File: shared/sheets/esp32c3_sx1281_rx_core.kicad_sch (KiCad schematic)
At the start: 36 parts, among them U1 ESP32-C3FH4, U2 TLV75533PDQNR, U3 SX1281IMLTRT, X1 CJ17-400001010B20

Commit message: Switch passives to 0201 with correct LCSC basic parts
- 100nF: C14858 (0201 X5R 6.3V)
- 1uF: C77857 (0201 X5R 6.3V)
- 10pF: C14854 (0201 C0G 25V)
- 470nF: C304534 (0201 X5R 6.3V)
- 1nF: C80390 (0201 X7R 25V)
- 10k: C172043 (0201 1%)
- 10uF: C15525 (0603 X5R 10V, no 0201 available)
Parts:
- C1, C13, C14, C15, C17, C2, C3, C4, C5: footprint Capacitor_SMD:C_0402_1005Metric -> Capacitor_SMD:C_0201_0603Metric; LCSC C1525 -> C14858
- C10, C19, C8, C9: footprint Capacitor_SMD:C_0402_1005Metric -> Capacitor_SMD:C_0201_0603Metric; LCSC C52923 -> C77857
- C16: footprint Capacitor_SMD:C_0402_1005Metric -> Capacitor_SMD:C_0201_0603Metric; LCSC C1543 -> C304534
- C18: footprint Capacitor_SMD:C_0402_1005Metric -> Capacitor_SMD:C_0201_0603Metric; LCSC C1523 -> C80390
- C6, C7: footprint Capacitor_SMD:C_0402_1005Metric -> Capacitor_SMD:C_0201_0603Metric; LCSC C32949 -> C14854
- R1, R2, R3, R4: footprint Resistor_SMD:R_0402_1005Metric -> Resistor_SMD:R_0201_0603Metric; LCSC C25744 -> C172043
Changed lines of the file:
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@@
 			)
 		)
-		(property "Footprint" "Capacitor_SMD:C_0402_1005Metric"
+		(property "Footprint" "Capacitor_SMD:C_0201_0603Metric"
 			(at 181.3052 120.65 0)
 			(hide yes)
@@
 			)
 		)
-		(property "LCSC" "C52923"
+		(property "LCSC" "C77857"
 			(at 0 0 0)
 			(show_name no)
@@
 			)
 		)
-		(property "Footprint" "Capacitor_SMD:C_0402_1005Metric"
+		(property "Footprint" "Capacitor_SMD:C_0201_0603Metric"
 			(at 158.4452 36.83 0)
 			(hide yes)
@@
 			)
 		)
-		(property "LCSC" "C1525"
+		(property "LCSC" "C14858"
 			(at 0 0 0)
 			(show_name no)
@@
 			)
 		)
-		(property "Footprint" "Capacitor_SMD:C_0402_1005Metric"
+		(property "Footprint" "Capacitor_SMD:C_0201_0603Metric"
 			(at 65.7352 93.98 0)
 			(hide yes)
@@
 			)
 		)
-		(property "LCSC" "C52923"
+		(property "LCSC" "C77857"
 			(at 0 0 0)
 			(show_name no)
@@
 			)
 		)
-		(property "Footprint" "Resistor_SMD:R_0402_1005Metric"
+		(property "Footprint" "Resistor_SMD:R_0201_0603Metric"
 			(at 62.992 78.74 90)
 			(hide yes)
@@
 			)
 		)
-		(property "LCSC" "C25744"
+		(property "LCSC" "C172043"
 			(at 0 0 0)
 			(show_name no)
@@
 			)
 		)
-		(property "Footprint" "Capacitor_SMD:C_0402_1005Metric"
+		(property "Footprint" "Capacitor_SMD:C_0201_0603Metric"
 			(at 74.6252 49.53 0)
 			(hide yes)
@@
 			)
 		)
-		(property "LCSC" "C32949"
+		(property "LCSC" "C14854"
 			(at 0 0 0)
 			(show_name no)
@@
 			)
 		)
-		(property "Footprint" "Capacitor_SMD:C_0402_1005Metric"
+		(property "Footprint" "Capacitor_SMD:C_0201_0603Metric"
 			(at 204.1652 64.77 0)
 			(hide yes)
@@
 			)
 		)
-		(property "LCSC" "C1525"
+		(property "LCSC" "C14858"
 			(at 0 0 0)
 			(show_name no)
@@
 			)
 		)
-		(property "Footprint" "Capacitor_SMD:C_0402_1005Metric"
+		(property "Footprint" "Capacitor_SMD:C_0201_0603Metric"
 			(at 38.4048 41.91 0)
 			(hide yes)
@@
 			)
 		)
-		(property "LCSC" "C32949"
+		(property "LCSC" "C14854"
 			(at 0 0 0)
 			(show_name no)
@@
 			)
 		)
-		(property "Footprint" "Capacitor_SMD:C_0402_1005Metric"
+		(property "Footprint" "Capacitor_SMD:C_0201_0603Metric"
 			(at 183.8452 36.83 0)
 			(hide yes)
@@
 			)
 		)
-		(property "LCSC" "C1525"
+		(property "LCSC" "C14858"
 			(at 0 0 0)
 			(show_name no)
@@
 			)
 		)
-		(property "Footprint" "Capacitor_SMD:C_0402_1005Metric"
+		(property "Footprint" "Capacitor_SMD:C_0201_0603Metric"
 			(at 243.84 76.5048 0)
 			(hide yes)
@@
 			)
 		)
-		(property "LCSC" "C1523"
+		(property "LCSC" "C80390"
 			(at 0 0 0)
 			(show_name no)
@@
 			)
 		)
-		(property "Footprint" "Resistor_SMD:R_0402_1005Metric"
+		(property "Footprint" "Resistor_SMD:R_0201_0603Metric"
 			(at 145.542 90.17 90)
 			(hide yes)
@@
 			)
 		)
-		(property "LCSC" "C25744"
+		(property "LCSC" "C172043"
 			(at 0 0 0)
 			(show_name no)
@@
 			)
 		)
-		(property "Footprint" "Resistor_SMD:R_0402_1005Metric"
+		(property "Footprint" "Resistor_SMD:R_0201_0603Metric"
 			(at 145.542 55.88 90)
 			(hide yes)
@@
 			)
 		)
-		(property "LCSC" "C25744"
+		(property "LCSC" "C172043"
 			(at 0 0 0)
 			(show_name no)
@@
 			)
 		)
-		(property "Footprint" "Capacitor_SMD:C_0402_1005Metric"
+		(property "Footprint" "Capacitor_SMD:C_0201_0603Metric"
 			(at 211.7852 120.65 0)
 			(hide yes)
@@
 			)
 		)
-		(property "LCSC" "C52923"
+		(property "LCSC" "C77857"
 			(at 0 0 0)
 			(show_name no)
@@
 			)
 		)
-		(property "Footprint" "Resistor_SMD:R_0402_1005Metric"
+		(property "Footprint" "Resistor_SMD:R_0201_0603Metric"
 			(at 70.612 78.74 90)
 			(hide yes)
@@
 			)
 		)
-		(property "LCSC" "C25744"
+		(property "LCSC" "C172043"
 			(at 0 0 0)
 			(show_name no)
@@
 			)
 		)
-		(property "Footprint" "Capacitor_SMD:C_0402_1005Metric"
+		(property "Footprint" "Capacitor_SMD:C_0201_0603Metric"
 			(at 196.5452 36.83 0)
 			(hide yes)
@@
 			)
 		)
-		(property "LCSC" "C1525"
+		(property "LCSC" "C14858"
 			(at 0 0 0)
 			(show_name no)
@@
 			)
 		)
-		(property "Footprint" "Capacitor_SMD:C_0402_1005Metric"
+		(property "Footprint" "Capacitor_SMD:C_0201_0603Metric"
 			(at 145.7452 36.83 0)
 			(hide yes)
@@
 			)
 		)
-		(property "LCSC" "C1525"
+		(property "LCSC" "C14858"
 			(at 0 0 0)
 			(show_name no)
@@
 			)
 		)
-		(property "Footprint" "Capacitor_SMD:C_0402_1005Metric"
+		(property "Footprint" "Capacitor_SMD:C_0201_0603Metric"
 			(at 223.2152 36.83 0)
 			(hide yes)
@@
 			)
 		)
-		(property "LCSC" "C1525"
+		(property "LCSC" "C14858"
 			(at 0 0 0)
 			(show_name no)
@@
 			)
 		)
-		(property "Footprint" "Capacitor_SMD:C_0402_1005Metric"
+		(property "Footprint" "Capacitor_SMD:C_0201_0603Metric"
 			(at 299.4152 36.83 0)
 			(hide yes)
@@
 			)
 		)
-		(property "LCSC" "C1543"
+		(property "LCSC" "C304534"
 			(at 0 0 0)
 			(show_name no)
@@
 			)
 		)
-		(property "Footprint" "Capacitor_SMD:C_0402_1005Metric"
+		(property "Footprint" "Capacitor_SMD:C_0201_0603Metric"
 			(at 80.9752 34.29 0)
 			(hide yes)
@@
 			)
 		)
-		(property "LCSC" "C52923"
+		(property "LCSC" "C77857"
 			(at 0 0 0)
 			(show_name no)
@@
 			)
 		)
-		(property "Footprint" "Capacitor_SMD:C_0402_1005Metric"
+		(property "Footprint" "Capacitor_SMD:C_0201_0603Metric"
 			(at 235.9152 36.83 0)
 			(hide yes)
@@
 			)
 		)
-		(property "LCSC" "C1525"
+		(property "LCSC" "C14858"
 			(at 0 0 0)
 			(show_name no)
@@
 			)
 		)
-		(property "Footprint" "Capacitor_SMD:C_0402_1005Metric"
+		(property "Footprint" "Capacitor_SMD:C_0201_0603Metric"
 			(at 210.5152 36.83 0)
 			(hide yes)
@@
 			)
 		)
-		(property "LCSC" "C1525"
+		(property "LCSC" "C14858"
 			(at 0 0 0)
 			(show_name no)
@@
 			)
 		)
-		(property "Footprint" "Capacitor_SMD:C_0402_1005Metric"
+		(property "Footprint" "Capacitor_SMD:C_0201_0603Metric"
 			(at 171.1452 36.83 0)
 			(hide yes)
@@
 			)
 		)
-		(property "LCSC" "C1525"
+		(property "LCSC" "C14858"
 			(at 0 0 0)
 			(show_name no)

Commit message: 10uF caps to 0402 (C15525), all other passives stay 0201
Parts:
- C11, C12: footprint Capacitor_SMD:C_0603_1608Metric -> Capacitor_SMD:C_0402_1005Metric
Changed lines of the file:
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@@
 			)
 		)
-		(property "Footprint" "Capacitor_SMD:C_0603_1608Metric"
+		(property "Footprint" "Capacitor_SMD:C_0402_1005Metric"
 			(at 169.8752 120.65 0)
 			(hide yes)
@@
 			)
 		)
-		(property "Footprint" "Capacitor_SMD:C_0603_1608Metric"
+		(property "Footprint" "Capacitor_SMD:C_0402_1005Metric"
 			(at 221.9452 120.65 0)
 			(hide yes)

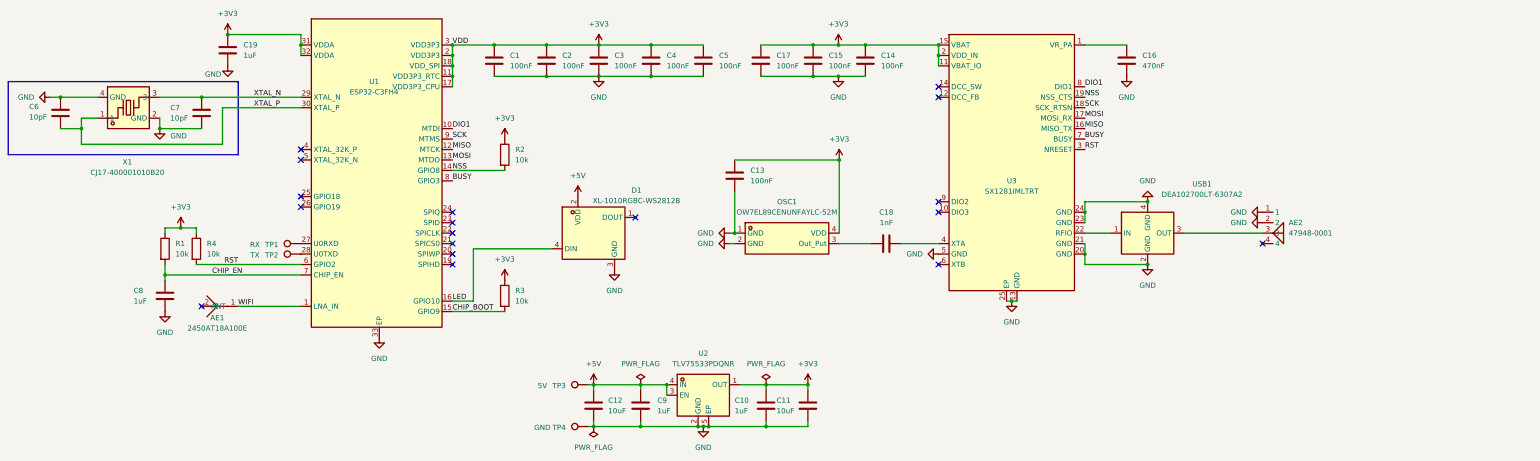
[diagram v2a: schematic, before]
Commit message: Add LCSC fields to all 24 passives in shared schematic
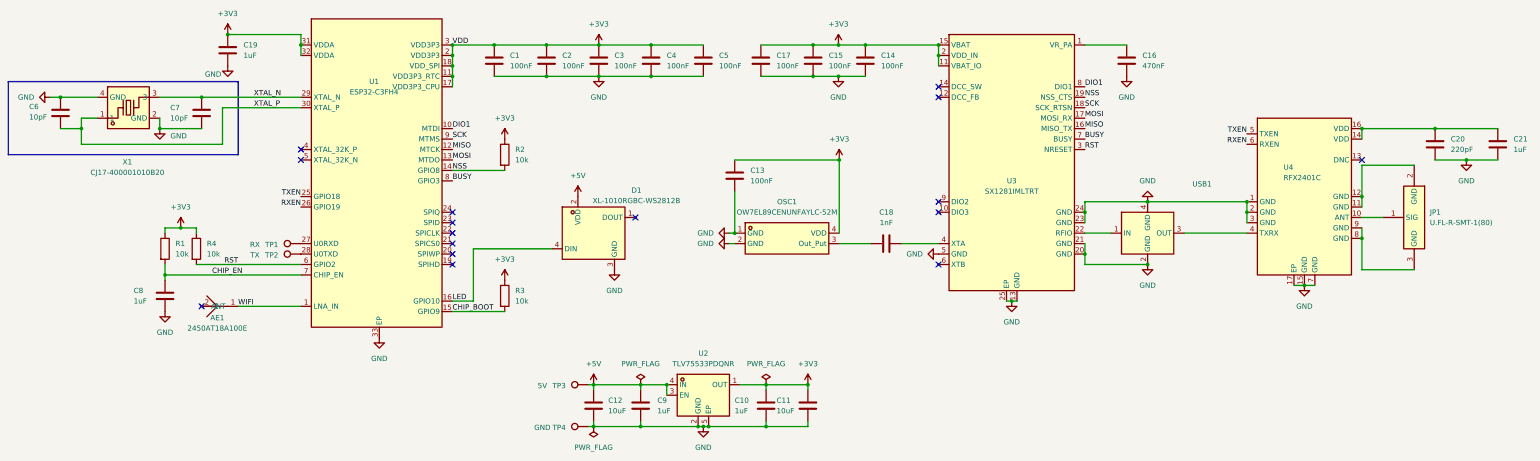
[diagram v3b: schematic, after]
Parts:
- removed AE2: 47948-0001, OpenRX-Shared:ANT-SMD_47948-0001, symbol OpenRX-Shared:47948-0001
- added C20: 220pF, Capacitor_SMD:C_0201_0603Metric, symbol Device:C
- added C21: 1uF, Capacitor_SMD:C_0201_0603Metric, symbol Device:C
- added JP1: U.FL-R-SMT-1(80), OpenRX-Shared:RF-SMD_FRF05002-JSS103M, symbol OpenRX-Shared:U.FL-R-SMT-1(80)
- added U4: RFX2401C, OpenRX-Shared:QFN-16_L3.0-W3.0-P0.50-BL-EP1.7, symbol OpenRX-Shared:RFX2401C
- C11, C12: footprint Capacitor_SMD:C_0402_1005Metric -> Capacitor_SMD:C_0201_0603Metric
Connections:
- net GND: now also C20.2, C21.2, U4.1 (GND), U4.15 (GND), U4.17 (EP), U4.2 (GND), U4.3 (GND), U4.7 (GND)
- net TXEN: now reaches U1.25 (GPIO18)
- net TXEN: now also U4.5 (TXEN)
- net RXEN: now reaches U1.26 (GPIO19)
- net RXEN: now also U4.6 (RXEN)
- net at USB1.3 (OUT): now also U4.4 (TXRX)
- new net: C20.1, C21.1, U4.14 (VDD), U4.16 (VDD)
- new net: JP1.1 (SIG), U4.10 (ANT)
- new net: JP1.2 (GND), U4.11 (GND), U4.12 (GND)
- new net: JP1.3 (GND), U4.8 (GND), U4.9 (GND)
- no-connect marks 18 -> 16
